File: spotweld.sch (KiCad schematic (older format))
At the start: 50 parts, among them J1 Conn_02x03_Odd_Even, J2 Conn_01x02, J3 Screw_Terminal_01x01, J4 Screw_Terminal_01x01, J5 Conn_01x02, Q1 IRF3205, Q2 IRF3205, Q3 IRF3205, Q4 IRF3205, Q5 IRF3205, Q6 IRF3205, Q7 IRF3205, Q8 IRF3205, SW1 SW_Push, U1 ATtiny24-20SSU, U2 TC4429VOA, U3 L78L05_SOT89

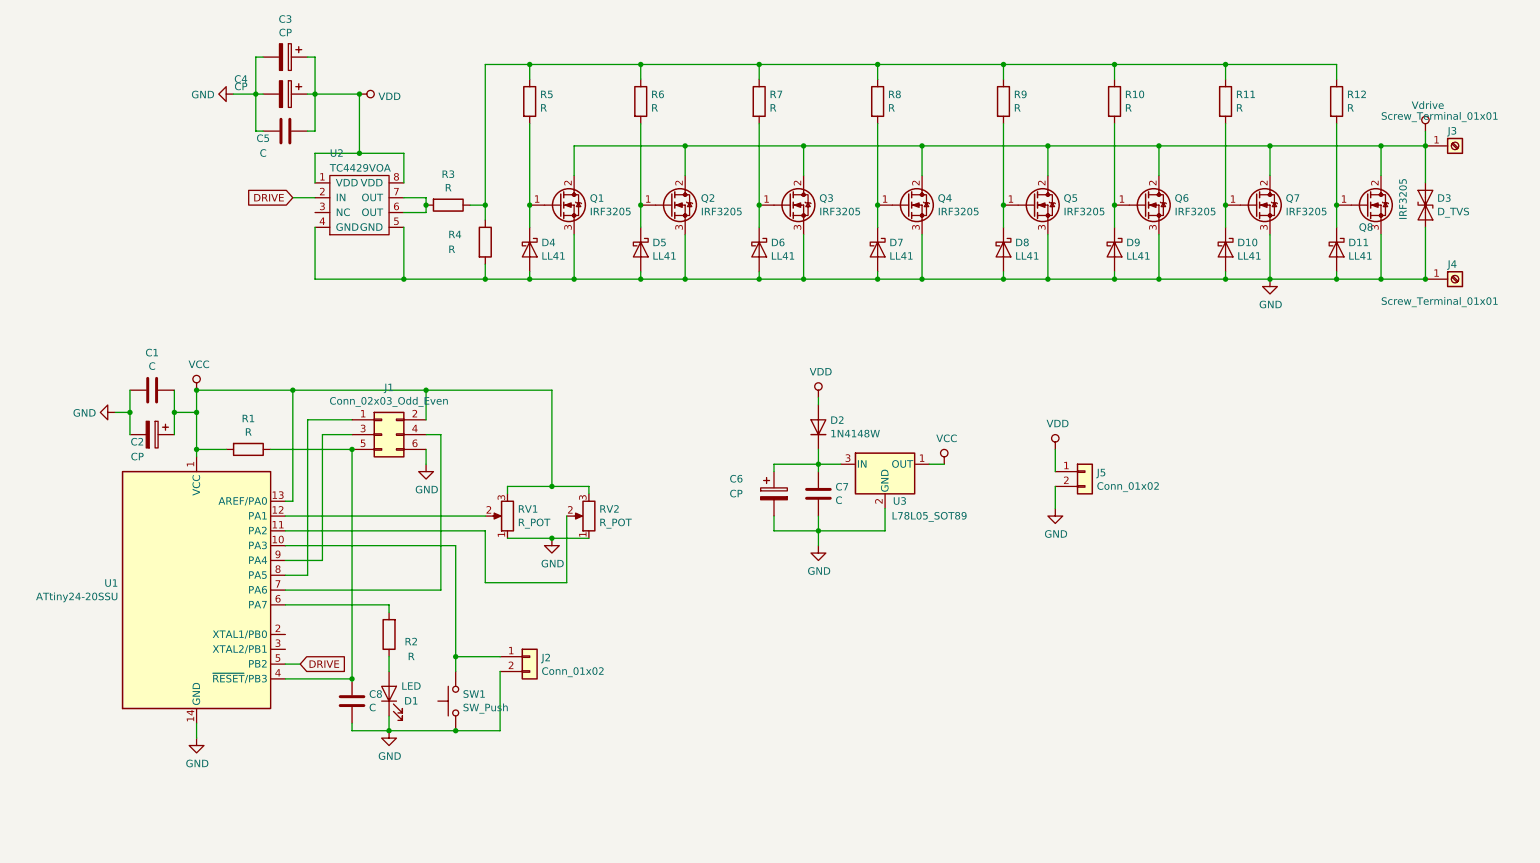
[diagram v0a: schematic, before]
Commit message: Update schematics component values
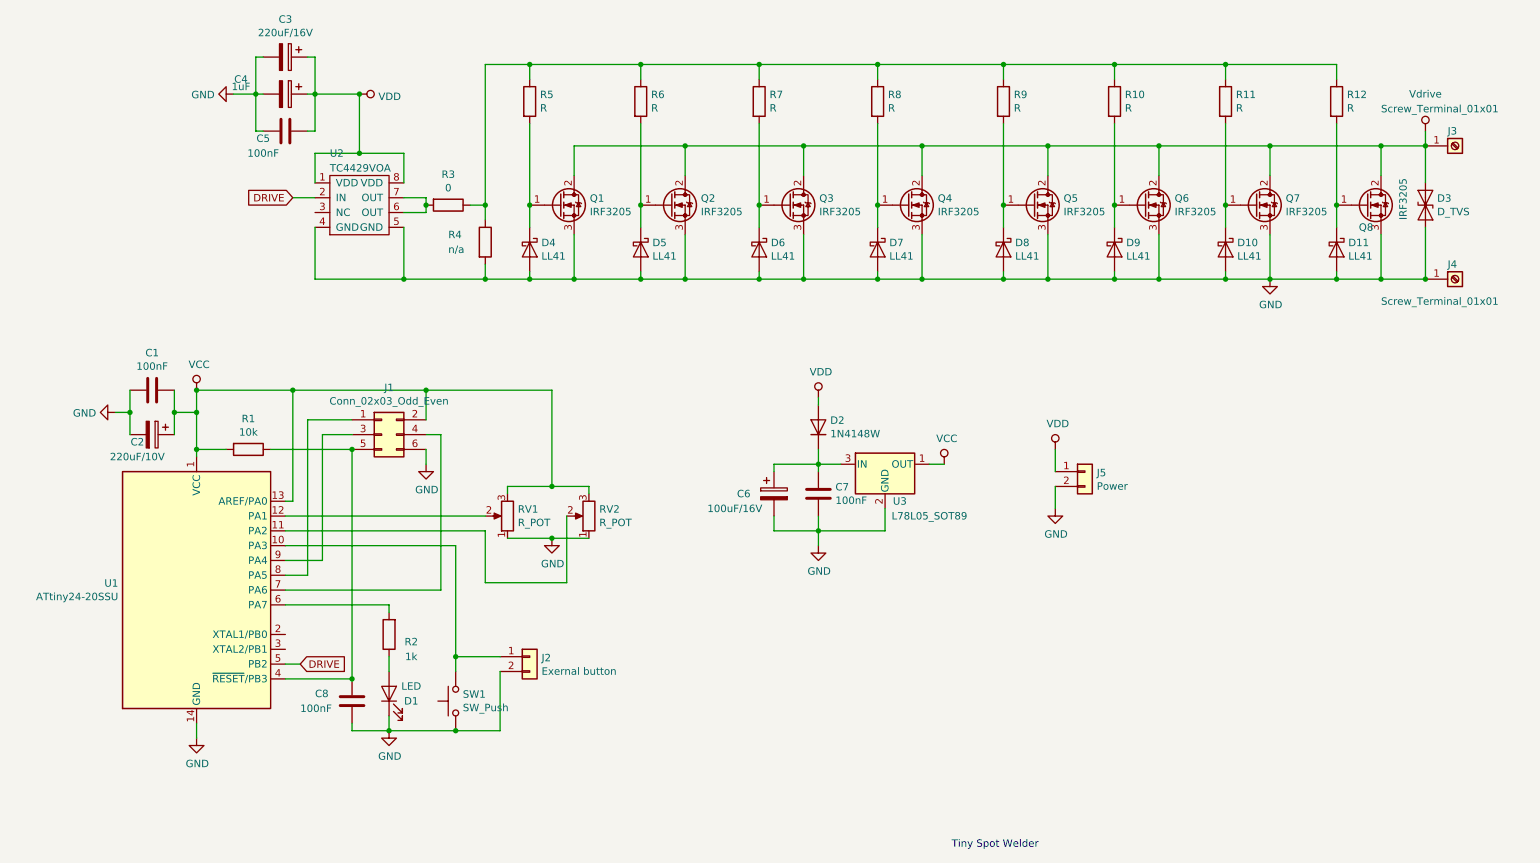
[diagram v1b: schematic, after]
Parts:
- C1, C5, C7, C8: value C -> 100nF
- C2: value CP -> 220uF/10V
- C3: value CP -> 220uF/16V
- C4: value CP -> 1uF
- C6: value CP -> 100uF/16V
- J2: value Conn_01x02 -> Exernal button
- J5: value Conn_01x02 -> Power
- R1: value R -> 10k
- R2: value R -> 1k
- R3: value R -> 0
- R4: value R -> n/a
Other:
- note added: "Tiny Spot Welder"
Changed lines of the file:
@@
 P 10850 2750
 F 0 "J3" H 10800 2850 50  0000 L CNN
-F 1 "Screw_Terminal_01x01" H 10350 2950 50  0000 L CNN
+F 1 "Screw_Terminal_01x01" H 10350 3000 50  0000 L CNN
 F 2 "" H 10850 2750 50  0001 C CNN
 F 3 "~" H 10850 2750 50  0001 C CNN
@@
 P 4300 3400
 F 0 "R4" H 4050 3450 50  0000 L CNN
-F 1 "R" H 4050 3350 50  0000 L CNN
+F 1 "n/a" H 4050 3350 50  0000 L CNN
 F 2 "Resistor_SMD:R_0805_2012Metric" V 4230 3400 50  0001 C CNN
 F 3 "~" H 4300 3400 50  0001 C CNN
@@
 P 4050 3150
 F 0 "R3" V 3843 3150 50  0000 C CNN
-F 1 "R" V 3934 3150 50  0000 C CNN
+F 1 "0" V 3934 3150 50  0000 C CNN
 F 2 "Resistor_SMD:R_0805_2012Metric" V 3980 3150 50  0001 C CNN
 F 3 "~" H 4050 3150 50  0001 C CNN
@@
 P 2950 2650
 F 0 "C5" V 2900 2800 50  0000 C CNN
-F 1 "C" V 2800 2800 50  0000 C CNN
+F 1 "100nF" V 2800 2800 50  0000 C CNN
 F 2 "Capacitor_SMD:C_0805_2012Metric" H 2988 2500 50  0001 C CNN
 F 3 "~" H 2950 2650 50  0001 C CNN
@@
 P 2950 2400
 F 0 "C4" V 2850 2100 50  0000 C CNN
-F 1 "CP" V 2900 2100 50  0000 C CNN
+F 1 "1uF" V 2900 2100 50  0000 C CNN
 F 2 "Capacitor_SMD:C_1206_3216Metric" H 2988 2250 50  0001 C CNN
 F 3 "~" H 2950 2400 50  0001 C CNN
@@
 P 2950 2150
 F 0 "C3" V 2695 2150 50  0000 C CNN
-F 1 "CP" V 2786 2150 50  0000 C CNN
+F 1 "220uF/16V" V 2786 2150 50  0000 C CNN
 F 2 "Capacitor_THT:CP_Radial_D8.0mm_P3.50mm" H 2988 2000 50  0001 C CNN
 F 3 "~" H 2950 2150 50  0001 C CNN
@@
 P 2700 4800
 F 0 "R1" V 2493 4800 50  0000 C CNN
-F 1 "R" V 2584 4800 50  0000 C CNN
+F 1 "10k" V 2584 4800 50  0000 C CNN
 F 2 "Resistor_SMD:R_0805_2012Metric" V 2630 4800 50  0001 C CNN
 F 3 "~" H 2700 4800 50  0001 C CNN
@@
 P 2050 4400
 F 0 "C1" V 1798 4400 50  0000 C CNN
-F 1 "C" V 1889 4400 50  0000 C CNN
+F 1 "100nF" V 1889 4400 50  0000 C CNN
 F 2 "Capacitor_SMD:C_0805_2012Metric" H 2088 4250 50  0001 C CNN
 F 3 "~" H 2050 4400 50  0001 C CNN
@@
 P 2050 4700
 F 0 "C2" V 2100 4600 50  0000 C CNN
-F 1 "CP" V 2200 4600 50  0000 C CNN
+F 1 "220uF/10V" V 2200 4600 50  0000 C CNN
 F 2 "Capacitor_THT:CP_Radial_D6.3mm_P2.50mm" H 2088 4550 50  0001 C CNN
 F 3 "~" H 2050 4700 50  0001 C CNN
@@
 P 3650 6050
 F 0 "R2" H 3500 6100 50  0000 C CNN
-F 1 "R" H 3500 6200 50  0000 C CNN
+F 1 "1k" H 3500 6200 50  0000 C CNN
 F 2 "Resistor_SMD:R_0805_2012Metric" V 3580 6050 50  0001 C CNN
 F 3 "~" H 3650 6050 50  0001 C CNN
@@
 P 6550 5100
 F 0 "C7" H 6665 5146 50  0000 L CNN
-F 1 "C" H 6665 5055 50  0000 L CNN
+F 1 "100nF" H 6665 5055 50  0000 L CNN
 F 2 "Capacitor_SMD:C_0805_2012Metric" H 6588 4950 50  0001 C CNN
 F 3 "~" H 6550 5100 50  0001 C CNN
@@
 U 1 1 5DA82FE4
 P 6250 5100
-F 0 "C6" H 5950 5200 50  0000 L CNN
-F 1 "CP" H 5950 5100 50  0000 L CNN
+F 0 "C6" H 6000 5100 50  0000 L CNN
+F 1 "100uF/16V" H 5800 5000 50  0000 L CNN
 F 2 "Capacitor_THT:CP_Radial_D6.3mm_P2.50mm" H 6288 4950 50  0001 C CNN
 F 3 "~" H 6250 5100 50  0001 C CNN
@@
 P 4600 6200
 F 0 "J2" H 4680 6192 50  0000 L CNN
-F 1 "Conn_01x02" H 4680 6101 50  0000 L CNN
+F 1 "Exernal button" H 4680 6101 50  0000 L CNN
 F 2 "Connector_PinHeader_2.54mm:PinHeader_1x02_P2.54mm_Vertical" H 4600 6200 50  0001 C CNN
 F 3 "~" H 4600 6200 50  0001 C CNN
@@
 P 8350 4950
 F 0 "J5" H 8430 4942 50  0000 L CNN
-F 1 "Conn_01x02" H 8430 4851 50  0000 L CNN
+F 1 "Power" H 8430 4851 50  0000 L CNN
 F 2 "Connector_PinHeader_2.54mm:PinHeader_1x02_P2.54mm_Vertical" H 8350 4950 50  0001 C CNN
 F 3 "~" H 8350 4950 50  0001 C CNN
@@
 P 10650 2650
 F 0 "#PWR015" H 10450 2500 50  0001 C CNN
-F 1 "Vdrive" H 10667 2823 50  0000 C CNN
+F 1 "Vdrive" H 10650 2900 50  0000 C CNN
 F 2 "" H 10650 2650 50  0001 C CNN
 F 3 "" H 10650 2650 50  0001 C CNN
@@
 U 1 1 5DEB7938
 P 3400 6500
-F 0 "C8" H 3515 6546 50  0000 L CNN
-F 1 "C" H 3515 6455 50  0000 L CNN
+F 0 "C8" H 3150 6550 50  0000 L CNN
+F 1 "100nF" H 3050 6450 50  0000 L CNN
 F 2 "Capacitor_SMD:C_0805_2012Metric" H 3438 6350 50  0001 C CNN
 F 3 "~" H 3400 6500 50  0001 C CNN
@@
 Wire Wire Line
 	3400 6700 3650 6700
+Text Notes 7450 7500 0    50   ~ 0
+Tiny Spot Welder
 $EndSCHEMATC
